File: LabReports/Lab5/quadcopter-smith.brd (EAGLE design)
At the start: 101.5 x 101.5 mm, 58 parts, among them J1 AVR_SPI_PRG_6NS, Q1 SI2302CDS, Q2 SI2302CDS, Q3 SI2302CDS, Q4 SI2302CDS, U1 ATMEGA128RFA1, U2 LSM9DS0-LGA24, Y1 16MHz

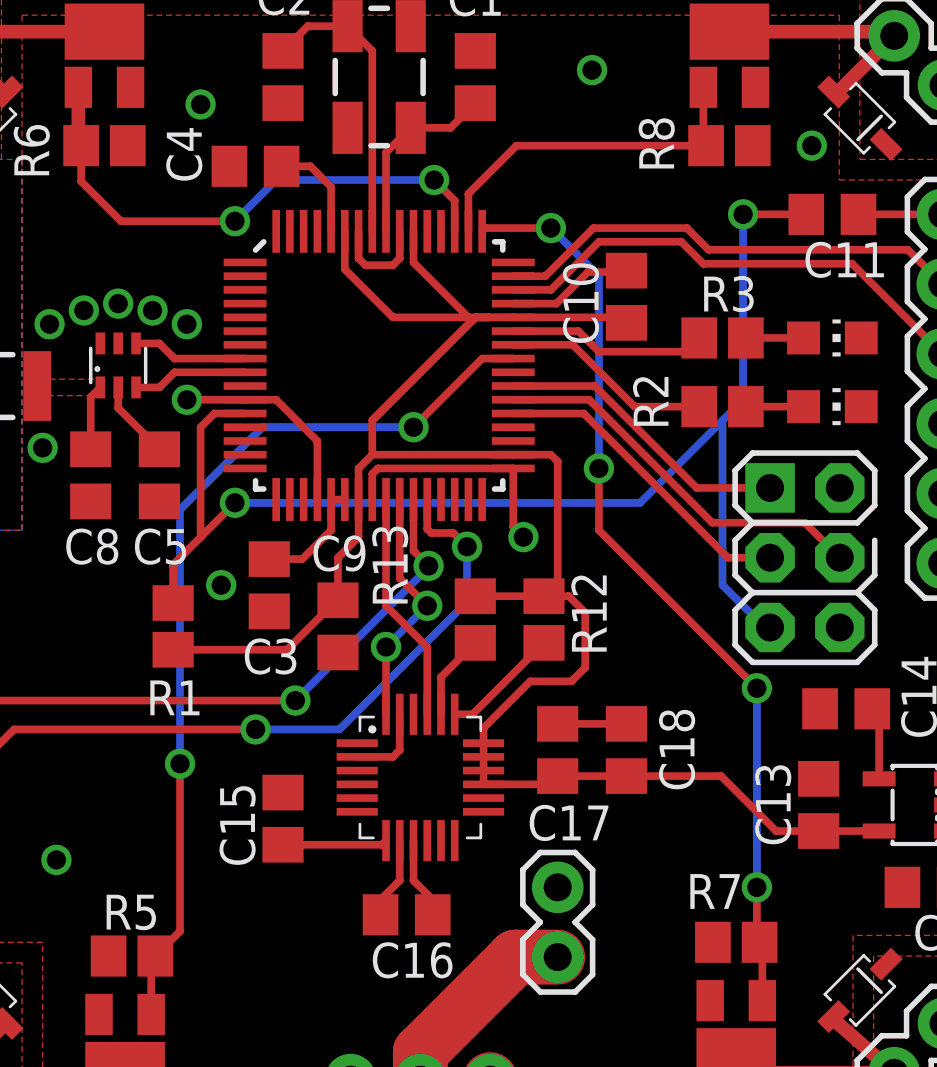
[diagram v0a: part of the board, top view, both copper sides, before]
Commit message: added logo and restrict under IMU
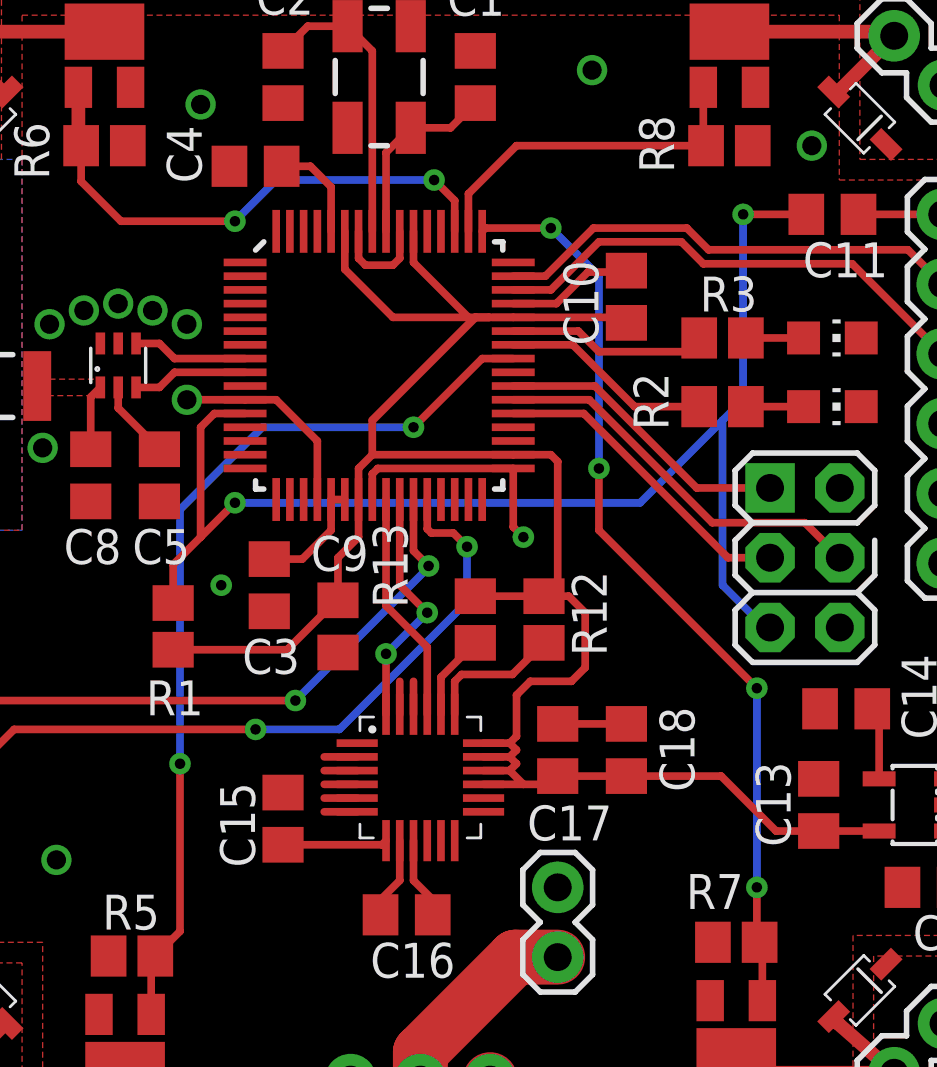
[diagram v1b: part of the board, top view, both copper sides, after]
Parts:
- added U$3: (no value), Trevor-lab4:LOGO
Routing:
- net GND: track 37.1 -> 42.5 mm
- net 3V: track 76.0 -> 79.1 mm
- net N$27: track 4.33 -> 5.03 mm
